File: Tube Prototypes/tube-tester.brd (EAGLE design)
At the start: 100 x 100 mm, 36 parts, among them IC1 NE555D, IC2 74141N, IC3 7805, Q1 IRF740S, Q2 BC546

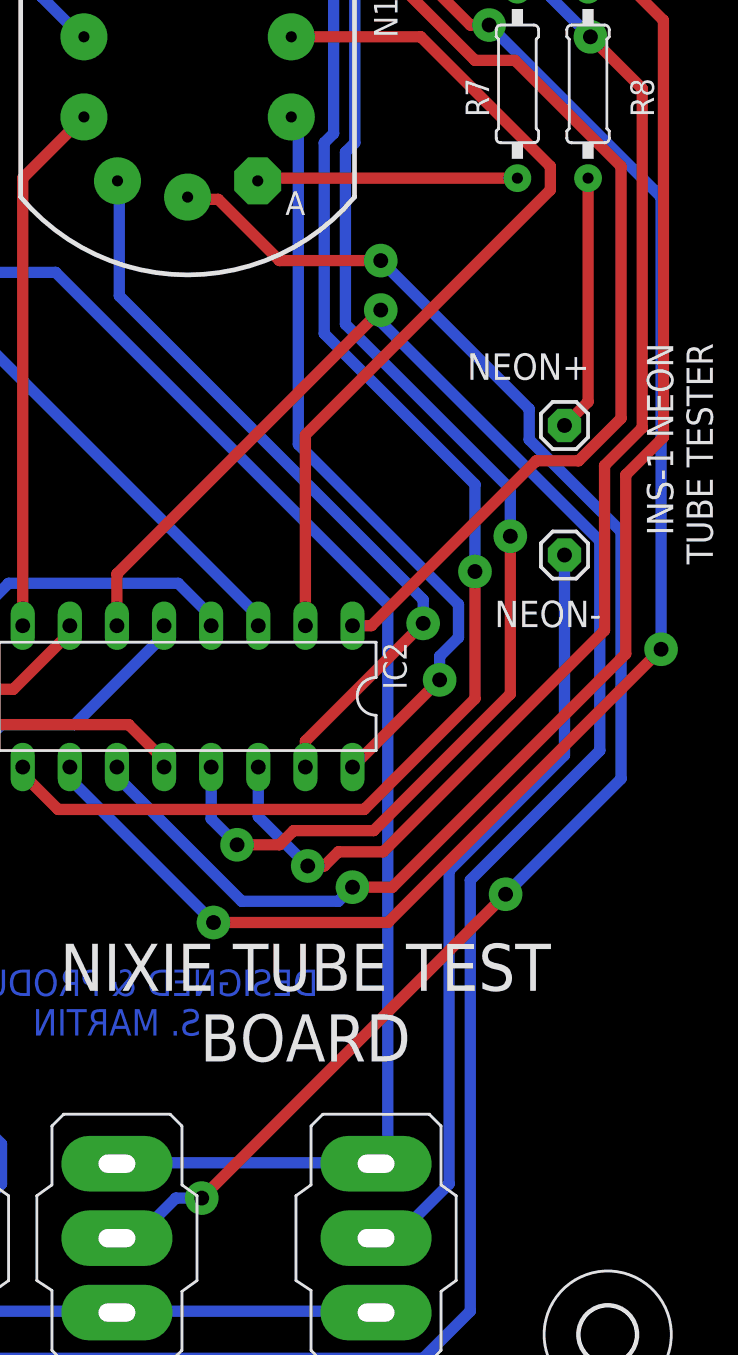
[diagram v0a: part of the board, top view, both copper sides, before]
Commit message: new prototype for dual tube board
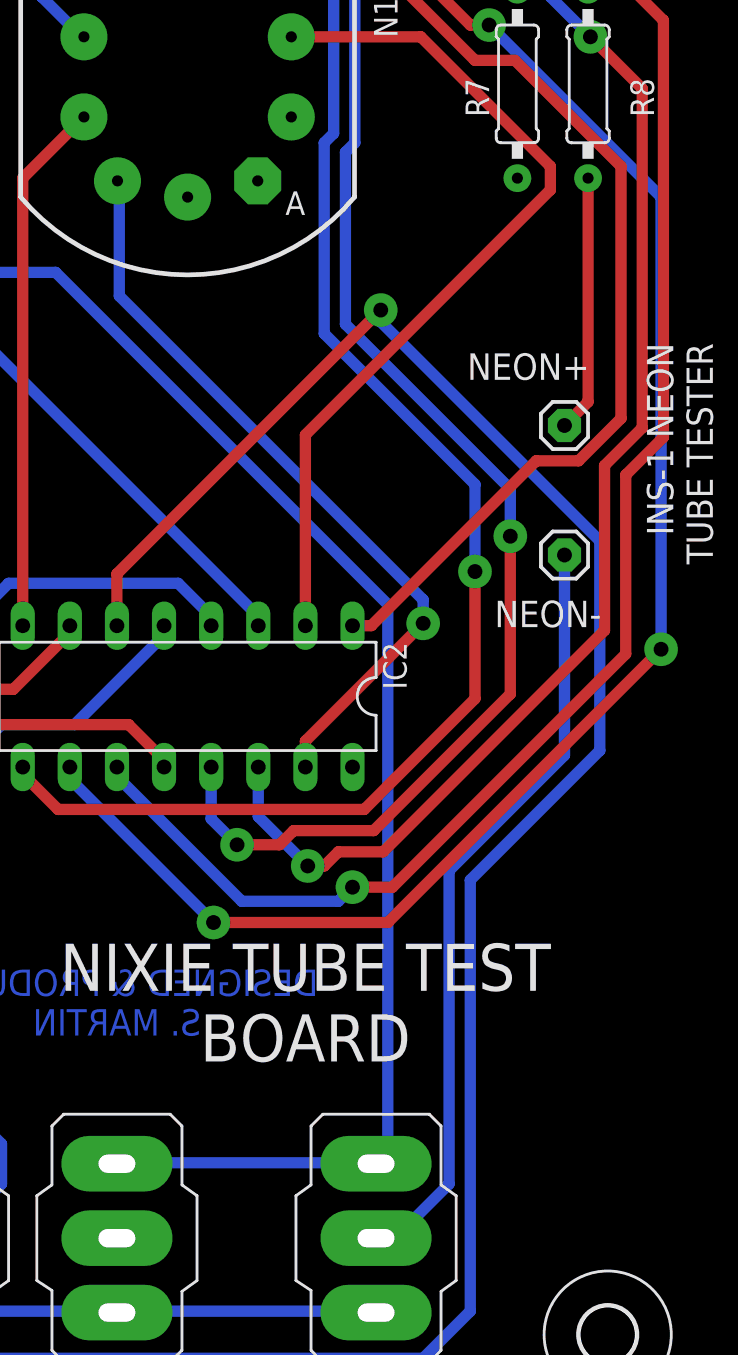
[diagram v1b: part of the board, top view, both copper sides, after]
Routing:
- net N$30: track 82.6 -> 0.00 mm, vias 3 -> 0
- net N$20: track 41.2 -> 0.00 mm, vias 1 -> 0
- net N$21: track 14.1 -> 0.00 mm
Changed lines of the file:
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@@
 <?xml version="1.0" encoding="utf-8"?>
 <!DOCTYPE eagle SYSTEM "eagle.dtd">
-<eagle version="6.4">
+<eagle version="6.6.0">
 <drawing>
 <settings>
@@
 <wire x1="75.44" y1="77.47" x2="82.423" y2="77.47" width="0.6096" layer="1"/>
 </signal>
-<signal name="N$20">
-<contactref element="N1" pad="0"/>
-<contactref element="IC2" pad="16"/>
-<wire x1="83.439" y1="42.799" x2="78.74" y2="38.1" width="0.6096" layer="1"/>
-<wire x1="83.439" y1="44.069" x2="83.439" y2="42.799" width="0.6096" layer="16"/>
-<wire x1="84.455" y1="45.085" x2="83.439" y2="44.069" width="0.6096" layer="16"/>
-<wire x1="84.455" y1="46.863" x2="84.455" y2="45.085" width="0.6096" layer="16"/>
-<wire x1="75.819" y1="55.499" x2="84.455" y2="46.863" width="0.6096" layer="16"/>
-<wire x1="75.819" y1="72.771" x2="75.819" y2="55.499" width="0.6096" layer="16"/>
-<wire x1="75.44" y1="73.15" x2="75.819" y2="72.771" width="0.6096" layer="16"/>
-<via x="83.439" y="42.799" extent="1-16" drill="0.8"/>
-</signal>
-<signal name="N$21">
-<contactref element="R7" pad="1"/>
-<contactref element="N1" pad="A"/>
-<wire x1="73.787" y1="69.85" x2="87.63" y2="69.85" width="0.6096" layer="1"/>
-<wire x1="73.66" y1="69.723" x2="73.787" y2="69.85" width="0.6096" layer="1"/>
-<wire x1="73.66" y1="69.723" x2="73.63" y2="69.704" width="0.6096" layer="1"/>
-</signal>
 <signal name="N$22">
 <contactref element="IC2" pad="3"/>
@@
 <wire x1="79.756" y1="16.764" x2="80.01" y2="16.7132" width="0.6096" layer="16"/>
 </signal>
+<signal name="N$20">
+<contactref element="N1" pad="0"/>
+<contactref element="IC2" pad="16"/>
+<wire x1="78.74" y1="38.1" x2="75.44" y2="73.15" width="0" layer="19" extent="1-1"/>
+</signal>
 <signal name="N$30">
+<contactref element="DP" pad="2"/>
 <contactref element="N1" pad="LHDP"/>
-<contactref element="DP" pad="2"/>
-<wire x1="71.501" y1="68.707" x2="69.85" y2="68.707" width="0.6096" layer="1"/>
-<wire x1="74.803" y1="65.405" x2="71.501" y2="68.707" width="0.6096" layer="1"/>
-<wire x1="80.264" y1="65.405" x2="74.803" y2="65.405" width="0.6096" layer="1"/>
-<wire x1="88.265" y1="57.404" x2="80.264" y2="65.405" width="0.6096" layer="16"/>
-<wire x1="88.265" y1="55.753" x2="88.265" y2="57.404" width="0.6096" layer="16"/>
-<wire x1="93.218" y1="50.8" x2="88.265" y2="55.753" width="0.6096" layer="16"/>
-<wire x1="93.218" y1="37.465" x2="93.218" y2="50.8" width="0.6096" layer="16"/>
-<wire x1="86.995" y1="31.242" x2="93.218" y2="37.465" width="0.6096" layer="16"/>
-<wire x1="70.612" y1="14.859" x2="86.995" y2="31.242" width="0.6096" layer="1"/>
-<wire x1="69.215" y1="14.859" x2="70.612" y2="14.859" width="0.6096" layer="16"/>
-<wire x1="67.056" y1="12.7" x2="69.215" y2="14.859" width="0.6096" layer="16"/>
-<wire x1="66.04" y1="12.7" x2="67.056" y2="12.7" width="0.6096" layer="16"/>
-<wire x1="69.85" y1="68.707" x2="69.85" y2="68.83" width="0.6096" layer="1"/>
-<via x="80.264" y="65.405" extent="1-16" drill="0.8"/>
-<via x="86.995" y="31.242" extent="1-16" drill="0.8"/>
-<via x="70.612" y="14.859" extent="1-16" drill="0.8"/>
+<wire x1="66.04" y1="12.7" x2="69.85" y2="68.83" width="0" layer="19" extent="1-1"/>
+</signal>
+<signal name="N$21">
+<contactref element="R7" pad="1"/>
+<contactref element="N1" pad="A"/>
+<wire x1="73.63" y1="69.704" x2="87.63" y2="69.85" width="0" layer="19" extent="1-1"/>
 </signal>
 </signals>
